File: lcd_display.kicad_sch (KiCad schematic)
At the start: 26 parts, among them P1 OrangePi-2G-IOT LCD Interface, U1 82357120100, U2 82357120100, U3 82357120100, U4 82357120100, U7 TPS61169DCKR, U8 AP2127K-2.8TRG1

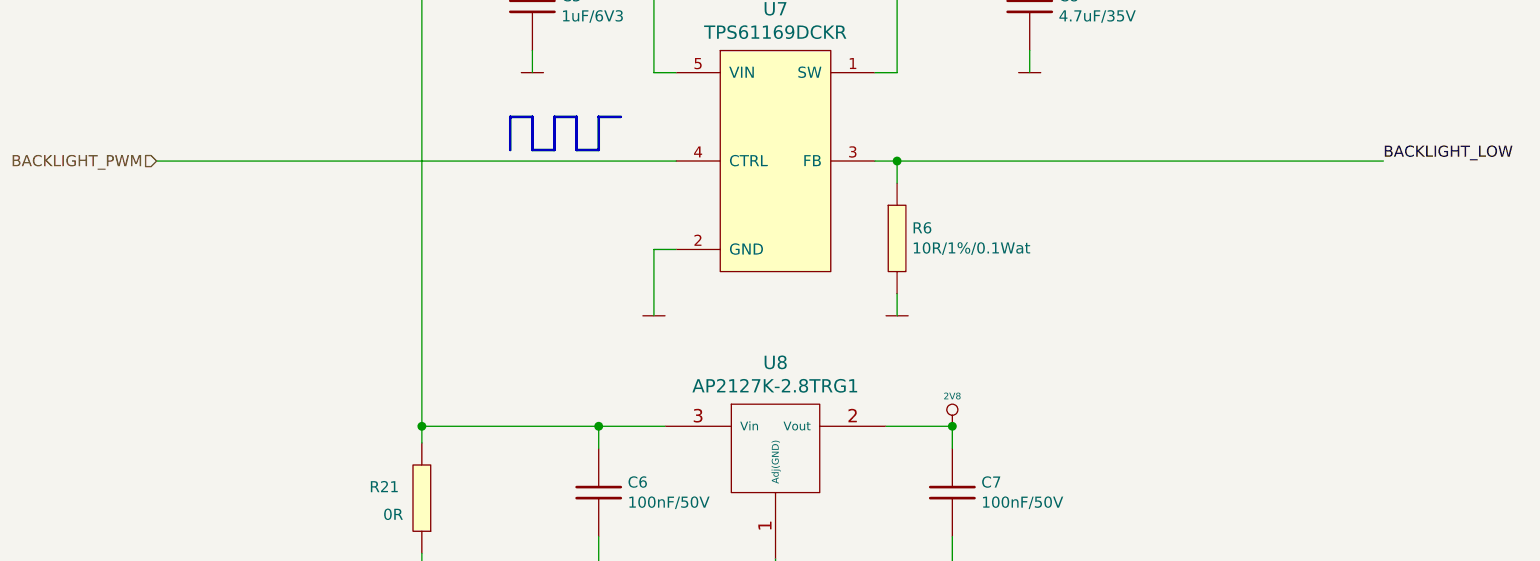
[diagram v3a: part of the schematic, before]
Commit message: Updated display pwm backlight section, regenerated gerbers again
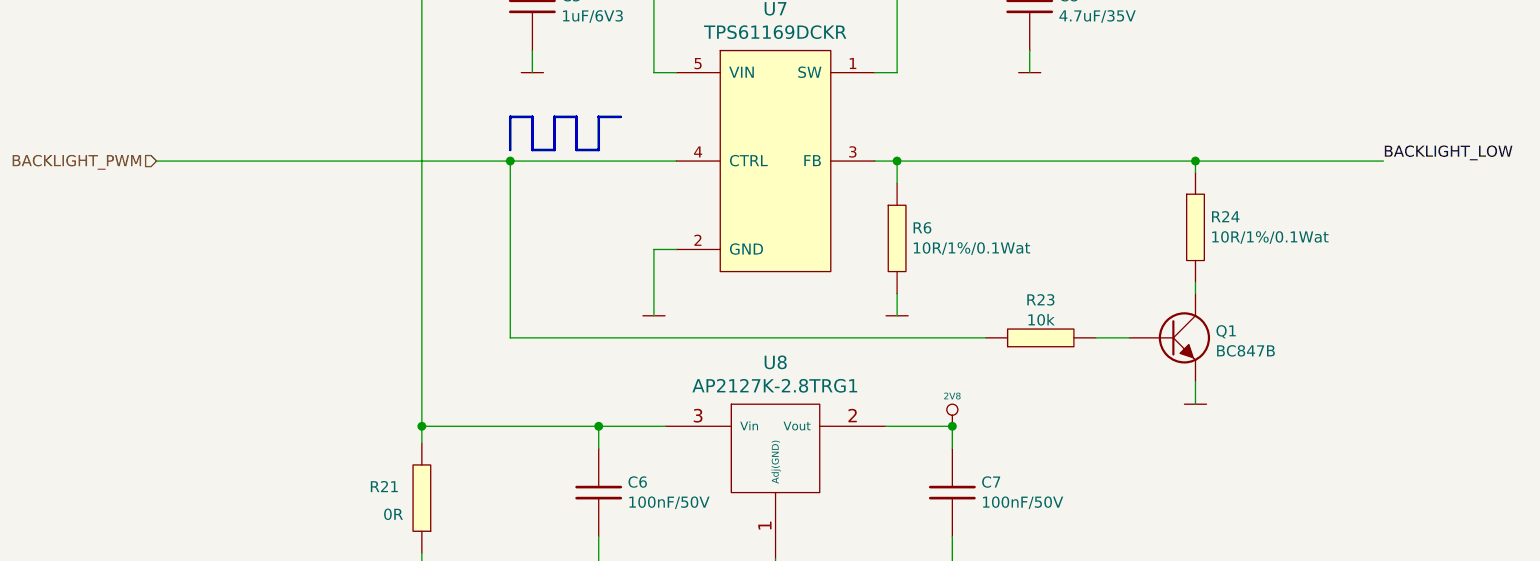
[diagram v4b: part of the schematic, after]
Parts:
- added Q1: BC847B, Transistor_Bipolar:BC847B_SOT23, symbol Transistor_Bipolar:BC847B
- added R23: 10k, Resistor_Smd_0603:10k_0603, symbol Resistors_Smd0603:10k
- added R24: 10R/1%/0.1Wat, Resistor_Smd_0603:10R_0603, symbol Resistors_Smd0603:10R_1%
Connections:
- net BACKLIGHT_LOW: now also R24.1
- net BACKLIGHT_PWM: now also R23.1
- net GND: now also Q1.2 (E)
- new net: Q1.1 (B), R23.2
- new net: Q1.3 (C), R24.2
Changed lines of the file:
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@@
   (junction (at 184.15 229.87) (diameter 1.016) (color 0 0 0 0))
   (junction (at 193.04 232.41) (diameter 1.016) (color 0 0 0 0))
+  (junction (at 194.31 73.66) (diameter 1.016) (color 0 0 0 0))
   (junction (at 196.85 48.26) (diameter 1.016) (color 0 0 0 0))
   (junction (at 201.93 234.95) (diameter 1.016) (color 0 0 0 0))
@@
   (junction (at 245.11 104.14) (diameter 1.016) (color 0 0 0 0))
   (junction (at 254 48.26) (diameter 1.016) (color 0 0 0 0))
+  (junction (at 273.05 73.66) (diameter 1.016) (color 0 0 0 0))
   (wire (pts (xy 101.6 217.17) (xy 101.6 218.44))
     (stroke (width 0) (type solid) (color 0 0 0 0))
@@
     (stroke (width 0) (type solid) (color 0 0 0 0))
   )
+  (wire (pts (xy 194.31 73.66) (xy 153.67 73.66))
+    (stroke (width 0) (type solid) (color 0 0 0 0))
+  )
+  (wire (pts (xy 194.31 73.66) (xy 194.31 93.98))
+    (stroke (width 0) (type solid) (color 0 0 0 0))
+  )
   (wire (pts (xy 196.85 48.26) (xy 184.15 48.26))
     (stroke (width 0) (type solid) (color 0 0 0 0))
@@
     (stroke (width 0) (type solid) (color 0 0 0 0))
   )
-  (wire (pts (xy 213.36 73.66) (xy 153.67 73.66))
+  (wire (pts (xy 213.36 73.66) (xy 194.31 73.66))
     (stroke (width 0) (type solid) (color 0 0 0 0))
   )
@@
     (stroke (width 0) (type solid) (color 0 0 0 0))
   )
-  (wire (pts (xy 238.76 73.66) (xy 294.64 73.66))
+  (wire (pts (xy 238.76 73.66) (xy 273.05 73.66))
     (stroke (width 0) (type solid) (color 0 0 0 0))
   )
@@
     (stroke (width 0) (type solid) (color 0 0 0 0))
   )
+  (wire (pts (xy 248.92 93.98) (xy 194.31 93.98))
+    (stroke (width 0) (type solid) (color 0 0 0 0))
+  )
   (wire (pts (xy 251.46 48.26) (xy 254 48.26))
     (stroke (width 0) (type solid) (color 0 0 0 0))
@@
   )
   (wire (pts (xy 254 60.96) (xy 254 63.5))
+    (stroke (width 0) (type solid) (color 0 0 0 0))
+  )
+  (wire (pts (xy 261.62 93.98) (xy 265.43 93.98))
+    (stroke (width 0) (type solid) (color 0 0 0 0))
+  )
+  (wire (pts (xy 273.05 73.66) (xy 273.05 74.93))
+    (stroke (width 0) (type solid) (color 0 0 0 0))
+  )
+  (wire (pts (xy 273.05 73.66) (xy 294.64 73.66))
+    (stroke (width 0) (type solid) (color 0 0 0 0))
+  )
+  (wire (pts (xy 273.05 87.63) (xy 273.05 88.9))
+    (stroke (width 0) (type solid) (color 0 0 0 0))
+  )
+  (wire (pts (xy 273.05 99.06) (xy 273.05 101.6))
     (stroke (width 0) (type solid) (color 0 0 0 0))
   )
@@
     )
     (property "Datasheet" "" (id 3) (at 254 63.5 0)
+      (effects (font (size 1.524 1.524)))
+    )
+    (pin "1")
+  )
+  (symbol (lib_id "power:GND") (at 273.05 101.6 0) (unit 1)
+    (in_bom yes) (on_board yes)
+    (property "Reference" "#PWR0149" (id 0) (at 273.05 99.06 0)
+      (effects (font (size 0.762 0.762)) hide)
+    )
+    (property "Value" "GND" (id 1) (at 273.05 104.14 0)
+      (effects (font (size 0.762 0.762)) hide)
+    )
+    (property "Footprint" "" (id 2) (at 273.05 101.6 0)
+      (effects (font (size 1.524 1.524)))
+    )
+    (property "Datasheet" "" (id 3) (at 273.05 101.6 0)
       (effects (font (size 1.524 1.524)))
     )
@@
     (pin "2")
   )
+  (symbol (lib_id "Resistors_Smd0603:10k") (at 255.27 93.98 90) (unit 1)
+    (in_bom yes) (on_board yes) (fields_autoplaced)
+    (property "Reference" "R23" (id 0) (at 255.27 89.6578 90))
+    (property "Value" "10k" (id 1) (at 255.27 91.9565 90))
+    (property "Footprint" "Resistor_Smd_0603:10k_0603" (id 2) (at 255.27 93.98 0)
+      (effects (font (size 1.524 1.524)) hide)
+    )
+    (property "Datasheet" "Resistors/Smd_0603/Components_Documentation/Vishay_Resistors_SM0603.pdf" (id 3) (at 255.27 93.98 0)
+      (effects (font (size 1.524 1.524)) hide)
+    )
+    (property "Manufacturer" "ROYAL OHM" (id 4) (at 255.27 93.98 0)
+      (effects (font (size 1.27 1.27)) hide)
+    )
+    (property "Manufacturer Part Number" "0603SAJ0103T5E" (id 5) (at 255.27 93.98 0)
+      (effects (font (size 1.27 1.27)) hide)
+    )
+    (property "Supplier" "TME" (id 6) (at 255.27 93.98 0)
+      (effects (font (size 1.27 1.27)) hide)
+    )
+    (property "Supplier Part Number" "SMD0603-10K" (id 7) (at 255.27 93.98 0)
+      (effects (font (size 1.27 1.27)) hide)
+    )
+    (property "URL" "https://www.tme.eu/pl/details/smd0603-10k/rezystory-smd-0603/royal-ohm/0603saj0103t5e/" (id 8) (at 255.27 93.98 0)
+      (effects (font (size 1.27 1.27)) hide)
+    )
+    (property "Price@1pc" "0,04560" (id 9) (at 255.27 93.98 0)
+      (effects (font (size 1.27 1.27)) hide)
+    )
+    (property "Price@1000pcs" "0,01111" (id 10) (at 255.27 93.98 0)
+      (effects (font (size 1.27 1.27)) hide)
+    )
+    (property "Developer" "MW" (id 11) (at 255.27 93.98 0)
+      (effects (font (size 1.27 1.27)) hide)
+    )
+    (property "Package" "0603" (id 12) (at 255.27 93.98 0)
+      (effects (font (size 1.27 1.27)) hide)
+    )
+    (pin "1")
+    (pin "2")
+  )
+  (symbol (lib_id "Resistors_Smd0603:10R_1%") (at 273.05 81.28 0) (unit 1)
+    (in_bom yes) (on_board yes)
+    (property "Reference" "R24" (id 0) (at 274.7772 80.1116 0)
+      (effects (font (size 1.27 1.27)) (justify left))
+    )
+    (property "Value" "10R/1%/0.1Wat" (id 1) (at 274.7772 82.423 0)
+      (effects (font (size 1.27 1.27)) (justify left))
+    )
+    (property "Footprint" "Resistor_Smd_0603:10R_0603" (id 2) (at 279.4 88.9 0)
+      (effects (font (size 1.27 1.27)) hide)
+    )
+    (property "Datasheet" "Resistors/Smd_0603/Components_Documentation/Panasonic_Precision_Resistors_SMD.pdf" (id 3) (at 279.4 88.9 0)
+      (effects (font (size 1.27 1.27)) hide)
+    )
+    (property "Manufacturer" "ROYAL OHM" (id 4) (at 273.05 81.28 0)
+      (effects (font (size 1.27 1.27)) hide)
+    )
+    (property "Manufacturer Part Number" "0603SAF100JT5E" (id 5) (at 273.05 81.28 0)
+      (effects (font (size 1.27 1.27)) hide)
+    )
+    (property "Supplier" "TME" (id 6) (at 273.05 81.28 0)
+      (effects (font (size 1.27 1.27)) hide)
+    )
+    (property "Supplier Part Number" "SMD0603-10R-1%" (id 7) (at 273.05 81.28 0)
+      (effects (font (size 1.27 1.27)) hide)
+    )
+    (property "URL" "https://www.tme.eu/pl/details/smd0603-10r-1%2525/rezystory-smd-0603/royal-ohm/0603saf100jt5e/" (id 8) (at 273.05 81.28 0)
+      (effects (font (size 1.27 1.27)) hide)
+    )
+    (property "Price@1pc" "0,06200" (id 9) (at 273.05 81.28 0)
+      (effects (font (size 1.27 1.27)) hide)
+    )
+    (property "Price@1000pcs" "0,01694" (id 10) (at 273.05 81.28 0)
+      (effects (font (size 1.27 1.27)) hide)
+    )
+    (property "Package" "0603" (id 11) (at 273.05 81.28 0)
+      (effects (font (size 1.27 1.27)) hide)
+    )
+    (property "Developer" "MW" (id 12) (at 273.05 81.28 0)
+      (effects (font (size 1.27 1.27)) hide)
+    )
+    (property "LCSC Part # (optional)" "C269702" (id 13) (at 273.05 81.28 0)
+      (effects (font (size 1.27 1.27)) hide)
+    )
+    (pin "1")
+    (pin "2")
+  )
   (symbol (lib_id "power:PWR_FLAG") (at 113.03 215.9 0) (unit 1)
     (in_bom yes) (on_board yes) (fields_autoplaced)
@@
     (pin "2")
   )
-  (symbol (lib_name "esd_protectors:82357120100_1") (lib_id "esd_protectors:82357120100") (at 193.04 250.19 90) (unit 1)
+  (symbol (lib_id "esd_protectors:82357120100") (at 193.04 250.19 90) (unit 1)
     (in_bom yes) (on_board yes)
     (property "Reference" "U2" (id 0) (at 194.3101 245.6191 90)
@@
     (pin "2")
   )
-  (symbol (lib_name "esd_protectors:82357120100_2") (lib_id "esd_protectors:82357120100") (at 201.93 250.19 90) (unit 1)
+  (symbol (lib_id "esd_protectors:82357120100") (at 201.93 250.19 90) (unit 1)
     (in_bom yes) (on_board yes)
     (property "Reference" "U3" (id 0) (at 203.2001 245.6191 90)
@@
     (pin "2")
   )
-  (symbol (lib_name "esd_protectors:82357120100_3") (lib_id "esd_protectors:82357120100") (at 210.82 250.19 90) (unit 1)
+  (symbol (lib_id "esd_protectors:82357120100") (at 210.82 250.19 90) (unit 1)
     (in_bom yes) (on_board yes)
     (property "Reference" "U4" (id 0) (at 212.0901 245.6191 90)
@@
     (pin "2")
   )
+  (symbol (lib_id "Transistor_Bipolar:BC847B") (at 270.51 93.98 0) (unit 1)
+    (in_bom yes) (on_board yes) (fields_autoplaced)
+    (property "Reference" "Q1" (id 0) (at 275.3615 93.2191 0)
+      (effects (font (size 1.27 1.27)) (justify left))
+    )
+    (property "Value" "BC847B" (id 1) (at 275.3615 95.5178 0)
+      (effects (font (size 1.27 1.27)) (justify left))
+    )
+    (property "Footprint" "Transistor_Bipolar:BC847B_SOT23" (id 2) (at 270.51 93.98 0)
+      (effects (font (size 1.524 1.524)) hide)
+    )
+    (property "Datasheet" "Transistors/Bipolar/Components_Documentation/BC84x(6_7).pdf" (id 3) (at 270.51 93.98 0)
+      (effects (font (size 1.524 1.524)) hide)
+    )
+    (property "Manufacturer" "	INFINEON TECHNOLOGIES" (id 4) (at 270.51 93.98 0)
+      (effects (font (size 1.27 1.27)) hide)
+    )
+    (property "Manufacturer Part Number" "BC847BE6327" (id 5) (at 270.51 93.98 0)
+      (effects (font (size 1.27 1.27)) hide)
+    )
+    (property "Supplier" "TME" (id 6) (at 270.51 93.98 0)
+      (effects (font (size 1.27 1.27)) hide)
+    )
+    (property "Supplier Part Number" "BC847BE6327" (id 7) (at 270.51 93.98 0)
+      (effects (font (size 1.27 1.27)) hide)
+    )
+    (property "URL" "https://www.tme.eu/pl/details/bc847be6327/tranzystory-npn-smd/infineon-technologies/" (id 8) (at 270.51 93.98 0)
+      (effects (font (size 1.27 1.27)) hide)
+    )
+    (property "Price@1pc" "0,1055" (id 9) (at 270.51 93.98 0)
+      (effects (font (size 1.27 1.27)) hide)
+    )
+    (property "Price@1000pcs" "0,0592" (id 10) (at 270.51 93.98 0)
+      (effects (font (size 1.27 1.27)) hide)
+    )
+    (property "Package" "SOT23-3" (id 11) (at 270.51 93.98 0)
+      (effects (font (size 1.27 1.27)) hide)
+    )
+    (pin "1")
+    (pin "2")
+    (pin "3")
+  )
   (symbol (lib_id "Linear_Regulators:AP2127K-2.8TRG1") (at 224.79 106.68 0) (unit 1)
